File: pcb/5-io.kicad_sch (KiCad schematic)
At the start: 33 parts, among them J501 TF PUSH, U501 TCA9555PWR

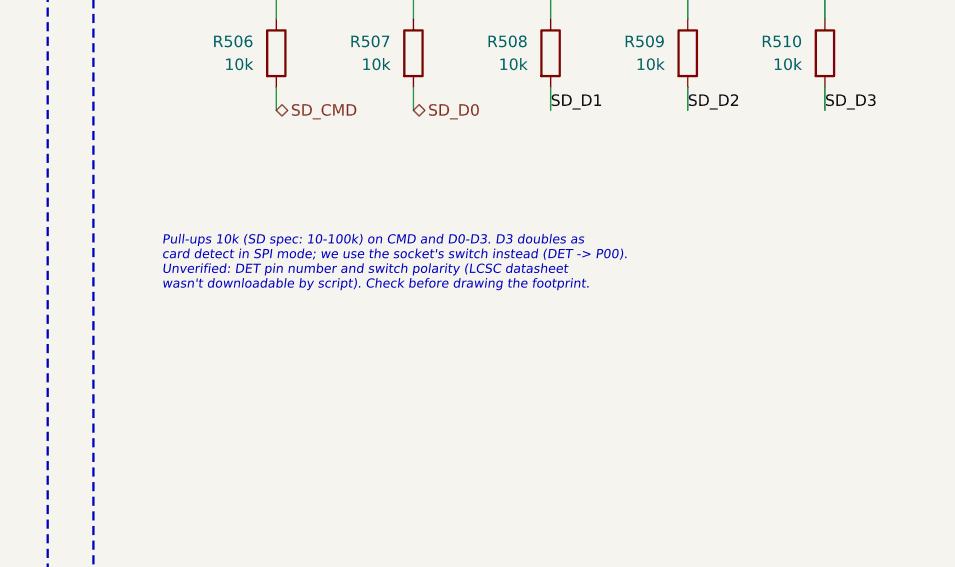
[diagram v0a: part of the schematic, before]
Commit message: Phase 3: footprint audit fixes and project footprint library
- New project footprint library pcb/scsi-adapter.pretty, generated by
  pcb/_gen/footprints.py from datasheet land patterns: TI RPW0010A (U101/U201),
  Kangnex WJ500V (J101), TE AMPLIMITE .050 HD50 (J302), SHOU HAN TF PUSH
  microSD (J501), Abracon AOTA-B201610 polarized inductor (L401), SHOU HAN
  2-pos DIP (SW301). fp-lib-table added.
- J303 LA header: 2x17 box header C20920, pins 33/34 NC (34-way ribbon to a
  future 2x16 adapter board).
- J302 HD50: TE 5787082-5 squeeze-latch receptacle; shielded symbol, shell to
  GND via R343 0R. TE STEP model git-ignored (pcb/scsi-adapter.3dshapes/).
- D101/D204/D605: D_SMF -> D_SOD-123F (parts are SOD-123FL).
- L401 pins swapped so pad 1 = polarity dot = DVDD_1V1 (RP2350 Fig. 23).
- SW401/SW402: Hroparts K2-1102DP C110153 on SW_PUSH_6mm.
- NOTES, decisions, sources updated; J601 pad question closed; RP2350B
  minimal-design layout copy planned (open question 17).
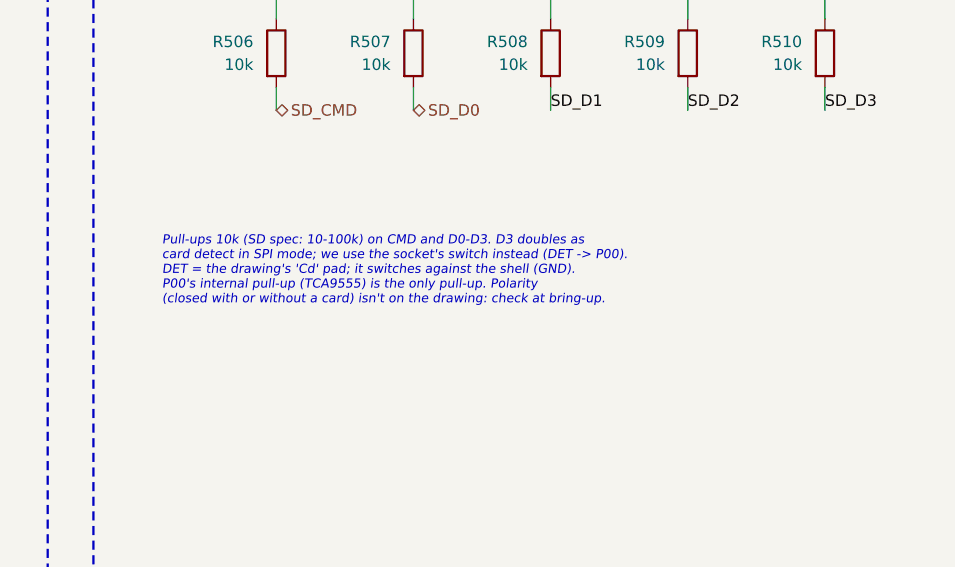
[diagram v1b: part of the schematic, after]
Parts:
- J501: footprint (none) -> scsi-adapter:microSD_SHOUHAN_TF-PUSH_PushPush_CardDetect
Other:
- note added: "Pull-ups 10k (SD spec: 10-100k) on CMD and D0-D3. D3 doubles as card detect in SPI mode; we use the socket's switch instead (DET -> P00). DET = the drawing's 'Cd' pad; it switches against the shell (GND). P00's internal pull-up (TCA9555) is the only pull-up. Polarity (closed with or without a card) isn't on the drawing: check at bring-up."
- note removed: "Pull-ups 10k (SD spec: 10-100k) on CMD and D0-D3. D3 doubles as card detect in SPI mode; we use the socket's switch instead (DET -> P00). Unverified: DET pin number and switch polarity (LCSC datasheet wasn't downloadable by script). Check before drawing the footprint."
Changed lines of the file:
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@@
 			(table_cell "P00 in" (exclude_from_sim no) (at 20.32 153.035 0) (size 22.86 4.445) (margins 0.9525 0.9525 0.9525 0.9525) (span 1 1) (fill (type none)) (effects (font (size 1.016 1.016)) (justify left top)))
 			(table_cell "SD_CARD_DETECT" (exclude_from_sim no) (at 43.18 153.035 0) (size 60.96 4.445) (margins 0.9525 0.9525 0.9525 0.9525) (span 1 1) (fill (type none)) (effects (font (size 1.016 1.016)) (justify left top)))
-			(table_cell "microSD card present (switch polarity: check the socket datasheet)" (exclude_from_sim no) (at 104.14 153.035 0) (size 142.24 4.445) (margins 0.9525 0.9525 0.9525 0.9525) (span 1 1) (fill (type none)) (effects (font (size 1.016 1.016)) (justify left top)))
+			(table_cell "microSD card switch (Cd to shell/GND; polarity: check at bring-up)" (exclude_from_sim no) (at 104.14 153.035 0) (size 142.24 4.445) (margins 0.9525 0.9525 0.9525 0.9525) (span 1 1) (fill (type none)) (effects (font (size 1.016 1.016)) (justify left top)))
 			(table_cell "P01 in" (exclude_from_sim no) (at 20.32 157.48 0) (size 22.86 4.445) (margins 0.9525 0.9525 0.9525 0.9525) (span 1 1) (fill (type none)) (effects (font (size 1.016 1.016)) (justify left top)))
 			(table_cell "TERMPWR_EN_INVERTED" (exclude_from_sim no) (at 43.18 157.48 0) (size 60.96 4.445) (margins 0.9525 0.9525 0.9525 0.9525) (span 1 1) (fill (type none)) (effects (font (size 1.016 1.016)) (justify left top)))
@@
 		(property "Reference" "J501" (at 335.28 68.58 0) (effects (font (size 1.27 1.27)) (justify left)))
 		(property "Value" "TF PUSH" (at 335.28 101.6 0) (effects (font (size 1.27 1.27)) (justify left)))
-		(property "Footprint" "" (at 355.6 83.82 0) (effects (font (size 1.27 1.27)) (hide yes)))
+		(property "Footprint" "scsi-adapter:microSD_SHOUHAN_TF-PUSH_PushPush_CardDetect" (at 355.6 83.82 0) (effects (font (size 1.27 1.27)) (hide yes)))
 		(property "Datasheet" "" (at 355.6 83.82 0) (effects (font (size 1.27 1.27)) (hide yes)))
-		(property "Description" "SHOU HAN TF PUSH, push-push with card detect. Footprint to do (EasyEDA/LCSC, checked against the drawing)." (at 355.6 83.82 0) (effects (font (size 1.27 1.27)) (hide yes)))
+		(property "Description" "SHOU HAN TF PUSH, push-push with card detect (Cd switches to the shell)" (at 355.6 83.82 0) (effects (font (size 1.27 1.27)) (hide yes)))
 		(property "LCSC" "C393941" (at 355.6 83.82 0) (effects (font (size 1.27 1.27)) (hide yes)))
 		(property "Fit" "JLC" (at 355.6 83.82 0) (effects (font (size 1.27 1.27)) (hide yes)))
@@
 		(instances (project "scsi-adapter" (path "/2c5b21a9-7d0d-4304-8bd9-0602cba3b7b5/e668c732-65b6-44b8-a62c-386a17bfcd95" (reference "#PWR525") (unit 1))))
 	)
-	(text "Pull-ups 10k (SD spec: 10-100k) on CMD and D0-D3. D3 doubles as\ncard detect in SPI mode; we use the socket's switch instead (DET -> P00).\nUnverified: DET pin number and switch polarity (LCSC datasheet\nwasn't downloadable by script). Check before drawing the footprint." (exclude_from_sim no) (at 266.7 160.02 0) (effects (font (size 1.016 1.016) (italic yes)) (justify left top)))
+	(text "Pull-ups 10k (SD spec: 10-100k) on CMD and D0-D3. D3 doubles as\ncard detect in SPI mode; we use the socket's switch instead (DET -> P00).\nDET = the drawing's 'Cd' pad; it switches against the shell (GND).\nP00's internal pull-up (TCA9555) is the only pull-up. Polarity\n(closed with or without a card) isn't on the drawing: check at bring-up." (exclude_from_sim no) (at 266.7 160.02 0) (effects (font (size 1.016 1.016) (italic yes)) (justify left top)))
 	(rectangle (start 200.66 203.2) (end 406.4 284.48) (stroke (width 0.254) (type dash)) (fill (type none)))
 	(text "Test points" (exclude_from_sim no) (at 208.28 210.82 0) (effects (font (size 2.0 2.0) (bold yes)) (justify left top)))

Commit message: route termpwr
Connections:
- net BENCH_EFUSE_FAULT_INVERTED is gone; now on net SD_CARD_DETECT: U501.7 (P03)
- net SD_CARD_DETECT: no longer U501.4 (P00)
- net TERMPWR_EFUSE_FAULT_INVERTED: now also U501.4 (P00)
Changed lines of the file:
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@@
 		)
 	)
-	(label "SD_CARD_DETECT"
+	(label "TERMPWR_EFUSE_FAULT_INVERTED"
 		(at 160.02 83.82 0)
 		(effects
@@
 		)
 	)
-	(hierarchical_label "BENCH_EFUSE_FAULT_INVERTED"
+	(hierarchical_label "SD_CARD_DETECT"
 		(shape input)
 		(at 160.02 91.44 0)

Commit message: more routing, mostly around the i2c expander and LEDs
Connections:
- net IS_BENCH_POWERED is gone; now on net LED_GREEN_INVERTED: U501.6 (P02)
- net LED_ACTIVITY_INVERTED: now also U501.9 (P05)
- net LED_GREEN_INVERTED: no longer U501.11 (P07)
- net LED_RED_INVERTED: now also U501.13 (P10), U501.8 (P04); no longer U501.9 (P05)
- net LED_STATUS_INVERTED: now also U501.10 (P06); no longer U501.13 (P10)
- net LED_YELLOW_INVERTED: now also U501.11 (P07), U501.7 (P03); no longer U501.10 (P06)
- net SD_CARD_DETECT: no longer U501.7 (P03)
- net TERMPWR_EFUSE_FAULT_INVERTED: no longer U501.8 (P04)
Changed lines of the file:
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@@
 		)
 	)
-	(label "LED_YELLOW_INVERTED"
+	(label "LED_STATUS_INVERTED"
 		(at 160.02 99.06 0)
 		(effects
@@
 		)
 	)
-	(label "LED_RED_INVERTED"
+	(label "LED_ACTIVITY_INVERTED"
 		(at 195.58 96.52 0)
 		(effects
@@
 		)
 	)
-	(label "LED_GREEN_INVERTED"
+	(label "LED_YELLOW_INVERTED"
 		(at 160.02 101.6 0)
 		(effects
@@
 		)
 	)
-	(label "LED_STATUS_INVERTED"
+	(label "LED_RED_INVERTED"
 		(at 160.02 106.68 0)
 		(effects
@@
 		)
 	)
-	(hierarchical_label "IS_BENCH_POWERED"
+	(hierarchical_label "LED_GREEN_INVERTED"
 		(shape input)
 		(at 160.02 88.9 0)
@@
 		)
 	)
-	(hierarchical_label "TERMPWR_EFUSE_FAULT_INVERTED"
+	(hierarchical_label "LED_RED_INVERTED"
 		(shape input)
 		(at 160.02 93.98 0)
@@
 		)
 	)
-	(hierarchical_label "SD_CARD_DETECT"
+	(hierarchical_label "LED_YELLOW_INVERTED"
 		(shape input)
 		(at 160.02 91.44 0)
